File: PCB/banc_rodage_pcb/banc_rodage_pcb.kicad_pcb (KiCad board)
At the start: 2 copper layers, 129 x 83 mm, 36 parts, among them J1 CONN_HALL, J10 CONN_THERMISTANCE_MOSFET_3, J11 CONN_THERMISTANCE_MOSFET_4, J12 CONN_NEXTION, J13 Conn_01x14_Pin, J2 CONN_MOTEUR, J3 CONN_ALIM, J4 CONN_CHAUFFE, J5 CONN_VENTIL, J6 CONN_THERMISTANCE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

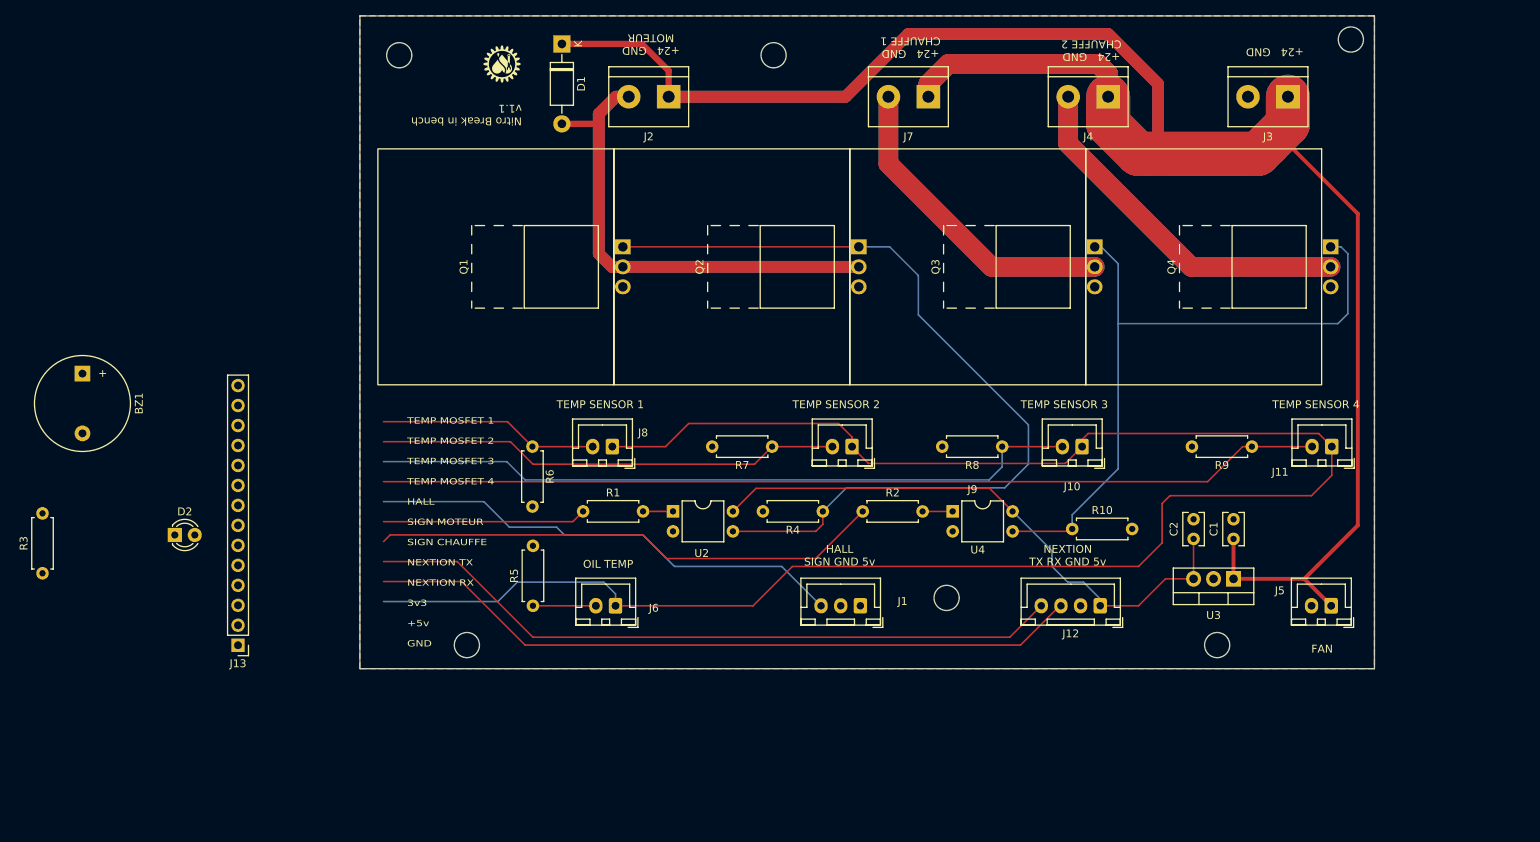
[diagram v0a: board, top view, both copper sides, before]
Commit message: cleanup. automode : gestion of brenkin profile with the sd card (rename, duplicate, delete) is ok
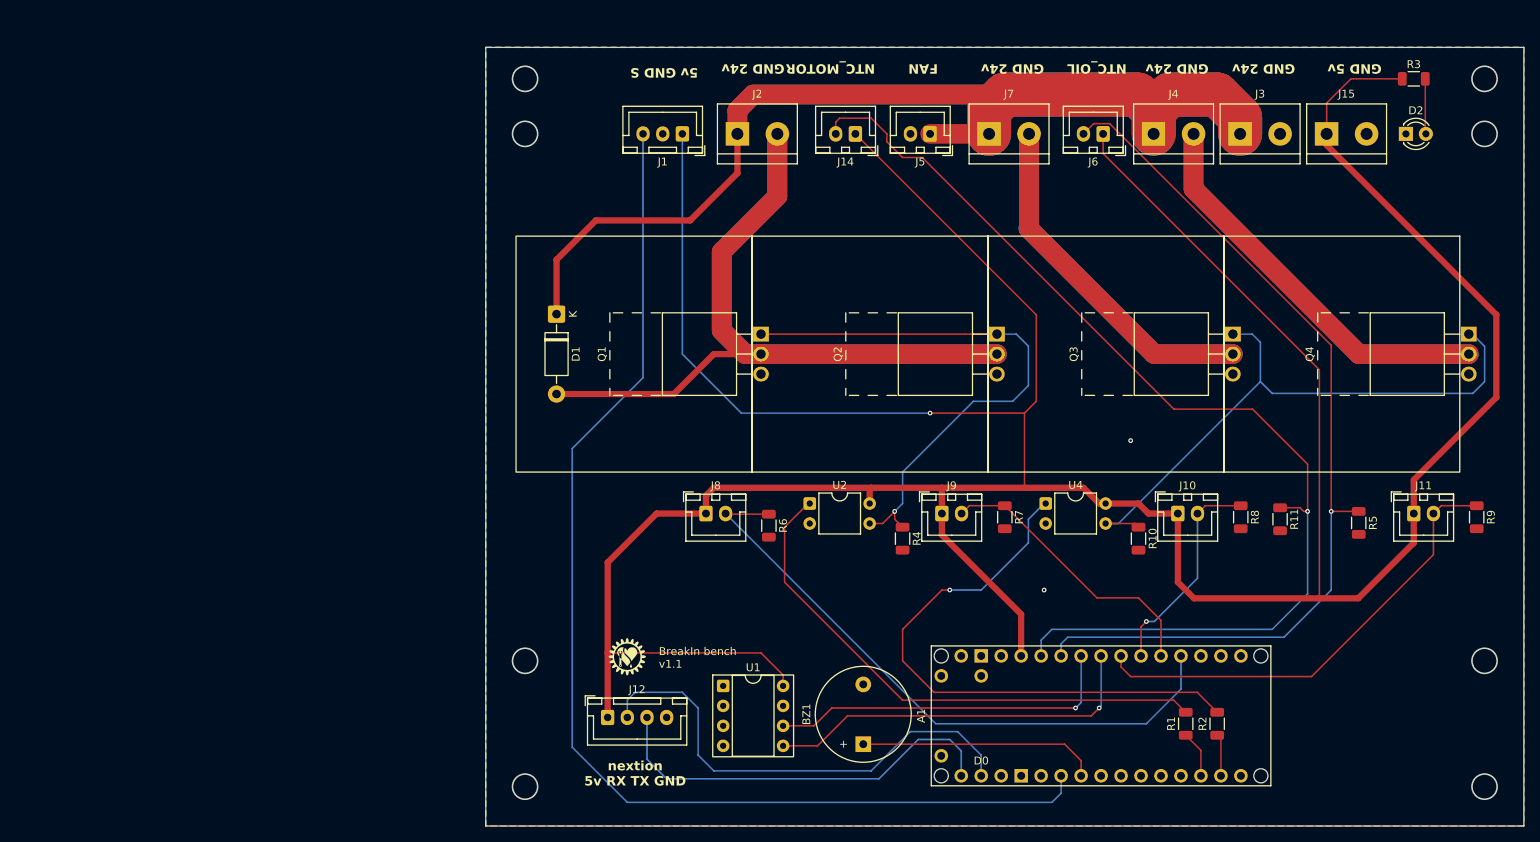
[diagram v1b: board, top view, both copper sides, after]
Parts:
- removed C1: 0.33uf, Capacitor_THT:C_Rect_L4.0mm_W2.5mm_P2.50mm
- removed C2: 0.1uf, Capacitor_THT:C_Rect_L4.0mm_W2.5mm_P2.50mm
- removed the G*** at (99.1, 38.1)
- removed J13: Conn_01x14_Pin, Connector_PinHeader_2.54mm:PinHeader_1x14_P2.54mm_Vertical
- removed U3: LM78M05_TO252, Package_TO_SOT_THT:TO-220-3_Vertical
- added A1: Arduino_Nano_R4, arduino nano r4:Arduino_Nano_R4, F.Cu at (196.8, 121.0)
- added G***: LOGO, perso:Logo, F.Cu at (115.0, 113.5)
- added J14: NTC_MOTOR, Connector_JST:JST_XH_B2B-XH-A_1x02_P2.50mm_Vertical, F.Cu at (144.0, 47.0)
- added J15: CONN_ALIM_5, perso:TerminalBlock_bornier-2_P5.08mm, F.Cu at (203.9, 47.0)
- added R11: 10K, Resistor_SMD:R_1206_3216Metric, F.Cu at (198.0, 96.0)
- added U1: CAT24C256, Package_DIP:DIP-8_W7.62mm_Socket, F.Cu at (127.2, 117.2)
- J10: value CONN_THERMISTANCE_MOSFET_3 -> NTC_MOSFET_3
- J11: value CONN_THERMISTANCE_MOSFET_4 -> NTC_MOSFET_4
- J2, J4, J7: footprint Perso:TerminalBlock_bornier-2_P5.08mm -> perso:TerminalBlock_bornier-2_P5.08mm
- J3: value CONN_ALIM -> CONN_ALIM_24; footprint Perso:TerminalBlock_bornier-2_P5.08mm -> perso:TerminalBlock_bornier-2_P5.08mm
- J6: value CONN_THERMISTANCE -> NTC_OIL
- J8: value CONN_THERMISTANCE_MOSFET_1 -> NTC_MOSFET_1
- J9: value CONN_THERMISTANCE_MOSFET_2 -> NTC_MOSFET_2
- Q1, Q2, Q3, Q4: footprint Perso:TO-220F-3_Horizontal_TabUp -> perso:TO-220F-3_Horizontal_TabUp
- R1, R10, R2, R3, R4, R5, R6, R7, R8, R9: footprint Resistor_THT:R_Axial_DIN0207_L6.3mm_D2.5mm_P7.62mm_Horizontal -> Resistor_SMD:R_1206_3216Metric
- moved R3 185.3 mm to (215.0, 40.0), turned to 0 degrees
- moved D2 164.6 mm to (214.0, 47.0)
- moved BZ1 109.9 mm to (145.0, 124.6), turned to 90 degrees
- moved R5 105.5 mm to (208.0, 96.5), turned to -90 degrees
- moved J6 86.3 mm to (175.5, 47.0)
- moved R1 81.2 mm to (186.0, 122.0), turned to 90 degrees
- moved J5 78.7 mm to (153.5, 47.0)
- moved J12 64.2 mm to (112.5, 121.2), turned to 0 degrees
- moved J1 64.1 mm to (122.0, 47.0)
- moved R2 52.5 mm to (190.0, 122.0), turned to 90 degrees
- moved D1 34.4 mm to (106.0, 69.9)
- moved R6 31.7 mm to (133.0, 96.8)
- moved R8 31.6 mm to (193.0, 95.7), turned to -90 degrees
- moved R7 30.9 mm to (163.0, 95.7), turned to -90 degrees
- moved R9 30.0 mm to (223.0, 95.7), turned to -90 degrees
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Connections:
- net /CHAUFFE_1 renamed /HEATER_1
- net /CHAUFFE_2 renamed /HEATER_2
- net /MOTEUR renamed /MOTOR
- net /SIGN_CHAUFFE renamed /SIGN_HEATER
- net /SIGN_MOTEUR renamed /SIGN_MOTOR
- net /SIGN_TEMP_HUILE renamed /PIN_NTC_OIL
- net /SIGN_THERMISTANCE_MOSFET_1 renamed /PIN_NTC_MOSFET_1
- net /SIGN_THERMISTANCE_MOSFET_2 renamed /PIN_NTC_MOSFET_2
- net /SIGN_THERMISTANCE_MOSFET_3 renamed /PIN_NTC_MOSFET_3
- net /SIGN_THERMISTANCE_MOSFET_4 renamed /PIN_NTC_MOSFET_4
- J1 pad 1: /3v3 -> +5V
- J10 pad 1: /3v3 -> +5V
- J11 pad 1: /3v3 -> +5V
- J12 pad 2: GND -> /NEXTION_TX
- J12 pad 4: /NEXTION_TX -> GND
- J6 pad 1: /3v3 -> +5V
- J8 pad 1: /3v3 -> +5V
- J9 pad 1: /3v3 -> +5V
- R1 pad 1: /ARDUINO_SIGN_MOTEUR -> /PIN_MOTOR
- R2 pad 1: /ARDUINO_SIGN_CHAUFFE -> /PIN_HEATER
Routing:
- net +5V: track 74.1 -> 474.1 mm, vias 0 -> 1
- net /3v3: track 235.5 -> 0.00 mm
- net +24V: track 379.4 -> 210.0 mm
- net /PIN_NTC_MOTOR: track 0.00 -> 139.0 mm, vias 0 -> 1
- net /PIN_NTC_OIL: track 7.66 -> 117.1 mm, vias 0 -> 1
- net /SIGN_HALL: track 61.1 -> 149.5 mm
- net Net-(R2-Pad2): track 3.82 -> 73.3 mm, vias 0 -> 1
- net Net-(R1-Pad2): track 3.81 -> 69.3 mm
- net /ARDUINO_SIGN_CHAUFFE: track 65.0 -> 0.00 mm
- net /PIN_NTC_MOSFET_3: track 90.5 -> 27.6 mm, vias 0 -> 1
- net /PIN_NTC_MOSFET_4: track 119.9 -> 59.2 mm
- net /PIN_NTC_MOSFET_1: track 27.9 -> 80.5 mm
- net Net-(A1-A4/SDA): track 0.00 -> 48.9 mm, vias 0 -> 1
- net Net-(A1-A5/SCL): track 0.00 -> 45.0 mm, vias 0 -> 1
- net /NEXTION_RX: track 91.6 -> 52.1 mm
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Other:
- board size 129 x 83 mm -> 132 x 99 mm
- board text added: "5v GND S"
- board text added: "BreakIn bench v1.1"
- board text added: "GND 24v"
- board text added: "GND 5v"
- board text added: "NTC_MOTOR"
- board text added: "NTC_OIL"
- board text added: "V1 : premiere edition v1.1 : ajout diode moteur, buzzer"
- board text added: "nextion 5v RX TX GND"
- board text removed: "+24 GND"
- board text removed: "+24 GND CHAUFFE 1"
- board text removed: "+24 GND CHAUFFE 2"
- board text removed: "+24 GND MOTEUR"
- board text removed: "HALL SIGN GND 5v"
- board text removed: "NEXTION TX RX GND 5v"
- board text removed: "Nitro Break in bench v1.1"
- board text removed: "OIL TEMP"
- board text removed: "TEMP MOSFET 1 TEMP MOSFET 2 TEMP MOSFET 3 TEMP MOSFET 4 HALL SIGN MOTEUR SIGN CHAUFFE NEXTION TX NEXTION RX 3v3 +5v GND"
- board text removed: "TEMP SENSOR 1"
- board text removed: "TEMP SENSOR 2"
- board text removed: "TEMP SENSOR 3"
- board text removed: "TEMP SENSOR 4"
- board text removed: "V1 : premiere edition v1.1 : ajout diode moteur"
